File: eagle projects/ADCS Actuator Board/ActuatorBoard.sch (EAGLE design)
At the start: 256 parts, among them J4 OSTVN08A150, J5 OSTVN08A150, J6 OSTVN08A150, U10 TVS991, U11 BD6210F-E2, U12 ADS7841E_2K5, U13 ADS7841E_2K5, U15 TLV9051IDCKR, U16 BD6210F-E2, U17 DRV10970_MOTOR_DRIVERDRV10970, U18 DRV10970_MOTOR_DRIVERDRV10970, U19 TLV9051IDCKR, U20 DRV10970_MOTOR_DRIVERDRV10970, U21 TLV9051IDCKR, U22 BD6210F-E2, U23 TLV9051IDCKR, U24 TLV9051IDCKR, U25 ADS7841E_2K5, U26 TLV9051IDCKR, U27 ADS7841E_2K5, U28 TLV9051IDCKR, U29 TLV9051IDCKR, U30 TLV9051IDCKR, U31 TLV9051IDCKR, U32 TLV9051IDCKR, U4 ADS7841E_2K5, U6 TLV9051IDCKR, U7 TVS991, U8 TVS991, U9 ADS7841E_2K5

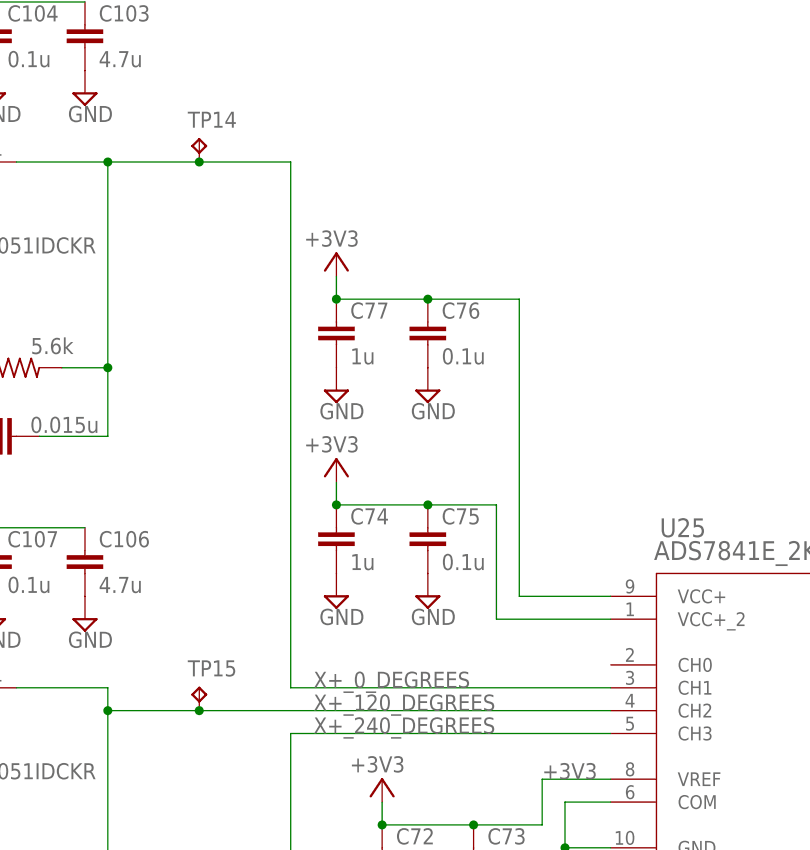
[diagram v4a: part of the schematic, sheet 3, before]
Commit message: finished rearranging analog side for minimal a/d ground bridge spacing
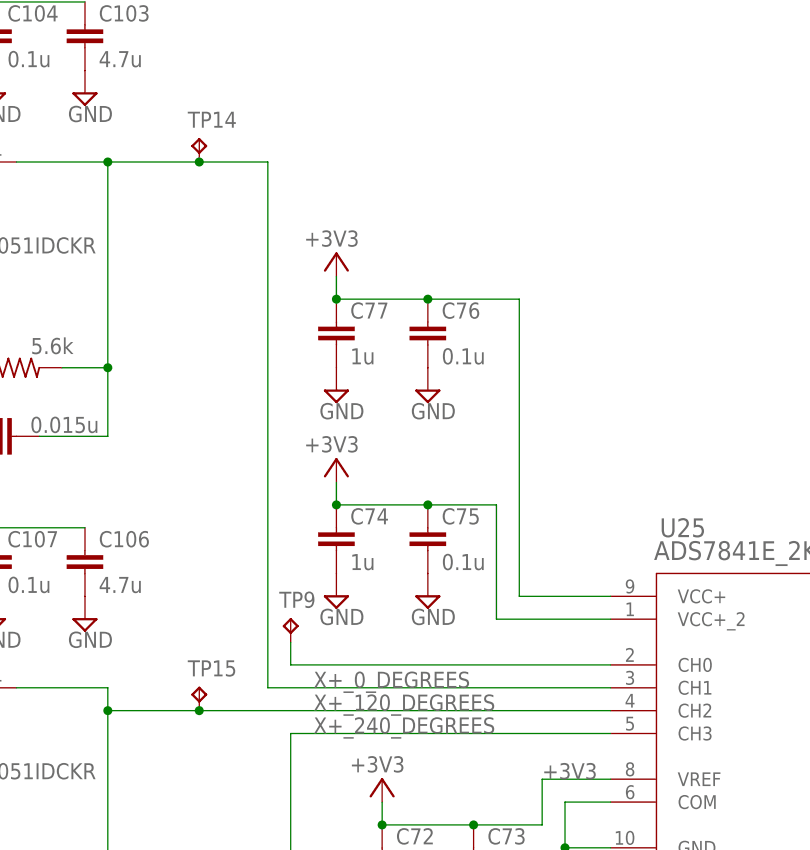
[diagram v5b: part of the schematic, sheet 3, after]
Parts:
- added TP1, TP13, TP17, TP9: TESTPOINT, my_library:TESTPOINT
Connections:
- new net N$1: TP1.TP, U13.CH0
- new net N$2: TP9.TP, U25.CH0
- new net N$3: TP13.TP, U27.CH0
- new net N$9: TP17.TP, U4.CH0
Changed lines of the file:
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@@
 <part name="R5" library="rcl" library_urn="urn:adsk.eagle:library:334" deviceset="R-US_" device="R0402" package3d_urn="urn:adsk.eagle:package:23547/3" value="10k"/>
 <part name="R6" library="rcl" library_urn="urn:adsk.eagle:library:334" deviceset="R-US_" device="R0402" package3d_urn="urn:adsk.eagle:package:23547/3" value="10k"/>
-<part name="JX" library="my_library" library_urn="urn:adsk.eagle:library:22876504" deviceset="TRM_BLK_1X2" device="" package3d_urn="urn:adsk.eagle:package:9320/1"/>
-<part name="JY" library="my_library" library_urn="urn:adsk.eagle:library:22876504" deviceset="TRM_BLK_1X2" device="" package3d_urn="urn:adsk.eagle:package:9320/1"/>
-<part name="JZ" library="my_library" library_urn="urn:adsk.eagle:library:22876504" deviceset="TRM_BLK_1X2" device="" package3d_urn="urn:adsk.eagle:package:9320/1"/>
+<part name="JX" library="my_library" library_urn="urn:adsk.eagle:library:22876504" deviceset="TRM_BLK_1X2" device="" package3d_urn="urn:adsk.eagle:package:26488321/2"/>
+<part name="JY" library="my_library" library_urn="urn:adsk.eagle:library:22876504" deviceset="TRM_BLK_1X2" device="" package3d_urn="urn:adsk.eagle:package:26488321/2"/>
+<part name="JZ" library="my_library" library_urn="urn:adsk.eagle:library:22876504" deviceset="TRM_BLK_1X2" device="" package3d_urn="urn:adsk.eagle:package:26488321/2"/>
 <part name="+3V4" library="supply1" library_urn="urn:adsk.eagle:library:371" deviceset="+3V3" device=""/>
 <part name="+3V6" library="supply1" library_urn="urn:adsk.eagle:library:371" deviceset="+3V3" device=""/>
@@
 <part name="C6" library="resistor" library_urn="urn:adsk.eagle:library:348" deviceset="C-EU" device="C0402" package3d_urn="urn:adsk.eagle:package:23626/2" value="4.7u"/>
 <part name="C7" library="resistor" library_urn="urn:adsk.eagle:library:348" deviceset="C-EU" device="C0402" package3d_urn="urn:adsk.eagle:package:23626/2" value="4.7u"/>
-<part name="J7" library="my_library" library_urn="urn:adsk.eagle:library:22876504" deviceset="TRM_BLK_1X2" device="" package3d_urn="urn:adsk.eagle:package:9320/1"/>
+<part name="J7" library="my_library" library_urn="urn:adsk.eagle:library:22876504" deviceset="TRM_BLK_1X2" device="" package3d_urn="urn:adsk.eagle:package:26488321/2"/>
+<part name="TP1" library="my_library" library_urn="urn:adsk.eagle:library:22876504" deviceset="TESTPOINT" device="" package3d_urn="urn:adsk.eagle:package:24605432/2"/>
+<part name="TP9" library="my_library" library_urn="urn:adsk.eagle:library:22876504" deviceset="TESTPOINT" device="" package3d_urn="urn:adsk.eagle:package:24605432/2"/>
+<part name="TP13" library="my_library" library_urn="urn:adsk.eagle:library:22876504" deviceset="TESTPOINT" device="" package3d_urn="urn:adsk.eagle:package:24605432/2"/>
+<part name="TP17" library="my_library" library_urn="urn:adsk.eagle:library:22876504" deviceset="TESTPOINT" device="" package3d_urn="urn:adsk.eagle:package:24605432/2"/>
 </parts>
 <sheets>
@@
 <attribute name="VALUE" x="240.03" y="98.298" size="1.778" layer="96"/>
 </instance>
+<instance part="TP9" gate="G$1" x="129.54" y="121.92" smashed="yes">
+<attribute name="NAME" x="128.27" y="123.19" size="1.778" layer="95"/>
+</instance>
 </instances>
 <busses>
@@
 <segment>
 <label x="132.08" y="114.3" size="1.778" layer="95"/>
-<wire x1="129.54" y1="172.72" x2="129.54" y2="114.3" width="0.1524" layer="91"/>
 <pinref part="U26" gate="G$1" pin="OUT"/>
 <wire x1="99.06" y1="172.72" x2="109.22" y2="172.72" width="0.1524" layer="91"/>
 <pinref part="R55" gate="G$1" pin="2"/>
 <wire x1="109.22" y1="172.72" x2="119.38" y2="172.72" width="0.1524" layer="91"/>
-<wire x1="119.38" y1="172.72" x2="129.54" y2="172.72" width="0.1524" layer="91"/>
+<wire x1="119.38" y1="172.72" x2="127" y2="172.72" width="0.1524" layer="91"/>
 <wire x1="104.14" y1="149.86" x2="109.22" y2="149.86" width="0.1524" layer="91"/>
 <wire x1="109.22" y1="149.86" x2="109.22" y2="172.72" width="0.1524" layer="91"/>
@@
 <wire x1="109.22" y1="142.24" x2="101.6" y2="142.24" width="0.1524" layer="91"/>
 <pinref part="U25" gate="A" pin="CH1"/>
-<wire x1="165.1" y1="114.3" x2="129.54" y2="114.3" width="0.1524" layer="91"/>
+<wire x1="165.1" y1="114.3" x2="127" y2="114.3" width="0.1524" layer="91"/>
+<wire x1="127" y1="114.3" x2="127" y2="172.72" width="0.1524" layer="91"/>
 </segment>
 </net>
@@
 </segment>
 </net>
+<net name="N$2" class="0">
+<segment>
+<pinref part="TP9" gate="G$1" pin="TP"/>
+<wire x1="129.54" y1="119.38" x2="129.54" y2="116.84" width="0.1524" layer="91"/>
+<pinref part="U25" gate="A" pin="CH0"/>
+<wire x1="129.54" y1="116.84" x2="165.1" y2="116.84" width="0.1524" layer="91"/>
+</segment>
+</net>
 </nets>
 </sheet>
@@
 <attribute name="VALUE" x="248.92" y="111.76" size="1.778" layer="96" rot="R180"/>
 </instance>
+<instance part="TP1" gate="G$1" x="121.92" y="124.46" smashed="yes">
+<attribute name="NAME" x="120.65" y="125.73" size="1.778" layer="95"/>
+</instance>
 </instances>
 <busses>
@@
 <segment>
 <label x="127" y="114.3" size="1.778" layer="95"/>
-<wire x1="124.46" y1="172.72" x2="124.46" y2="114.3" width="0.1524" layer="91"/>
+<wire x1="119.38" y1="172.72" x2="119.38" y2="114.3" width="0.1524" layer="91"/>
 <pinref part="U15" gate="G$1" pin="OUT"/>
 <wire x1="93.98" y1="172.72" x2="104.14" y2="172.72" width="0.1524" layer="91"/>
 <pinref part="R40" gate="G$1" pin="2"/>
 <wire x1="104.14" y1="172.72" x2="114.3" y2="172.72" width="0.1524" layer="91"/>
-<wire x1="114.3" y1="172.72" x2="124.46" y2="172.72" width="0.1524" layer="91"/>
+<wire x1="114.3" y1="172.72" x2="119.38" y2="172.72" width="0.1524" layer="91"/>
 <wire x1="99.06" y1="149.86" x2="104.14" y2="149.86" width="0.1524" layer="91"/>
 <wire x1="104.14" y1="149.86" x2="104.14" y2="172.72" width="0.1524" layer="91"/>
@@
 <wire x1="104.14" y1="142.24" x2="96.52" y2="142.24" width="0.1524" layer="91"/>
 <pinref part="U13" gate="A" pin="CH1"/>
-<wire x1="160.02" y1="114.3" x2="124.46" y2="114.3" width="0.1524" layer="91"/>
+<wire x1="160.02" y1="114.3" x2="119.38" y2="114.3" width="0.1524" layer="91"/>
 </segment>
 </net>
@@
 </segment>
 </net>
+<net name="N$1" class="0">
+<segment>
+<pinref part="U13" gate="A" pin="CH0"/>
+<wire x1="160.02" y1="116.84" x2="121.92" y2="116.84" width="0.1524" layer="91"/>
+<wire x1="121.92" y1="116.84" x2="121.92" y2="121.92" width="0.1524" layer="91"/>
+<pinref part="TP1" gate="G$1" pin="TP"/>
+</segment>
+</net>
 </nets>
 </sheet>
@@
 <attribute name="VALUE" x="121.92" y="165.1" size="1.778" layer="96" rot="R180"/>
 </instance>
+<instance part="TP13" gate="G$1" x="111.76" y="121.92" smashed="yes">
+<attribute name="NAME" x="110.49" y="123.19" size="1.778" layer="95"/>
+</instance>
 </instances>
 <busses>
@@
 <segment>
 <label x="116.84" y="114.3" size="1.778" layer="95"/>
-<wire x1="114.3" y1="172.72" x2="114.3" y2="114.3" width="0.1524" layer="91"/>
+<wire x1="109.22" y1="172.72" x2="109.22" y2="114.3" width="0.1524" layer="91"/>
 <pinref part="U30" gate="G$1" pin="OUT"/>
 <wire x1="83.82" y1="172.72" x2="93.98" y2="172.72" width="0.1524" layer="91"/>
 <pinref part="R64" gate="G$1" pin="2"/>
 <wire x1="93.98" y1="172.72" x2="104.14" y2="172.72" width="0.1524" layer="91"/>
-<wire x1="104.14" y1="172.72" x2="114.3" y2="172.72" width="0.1524" layer="91"/>
+<wire x1="104.14" y1="172.72" x2="109.22" y2="172.72" width="0.1524" layer="91"/>
 <wire x1="88.9" y1="149.86" x2="93.98" y2="149.86" width="0.1524" layer="91"/>
 <wire x1="93.98" y1="149.86" x2="93.98" y2="172.72" width="0.1524" layer="91"/>
@@
 <wire x1="93.98" y1="142.24" x2="86.36" y2="142.24" width="0.1524" layer="91"/>
 <pinref part="U27" gate="A" pin="CH1"/>
-<wire x1="149.86" y1="114.3" x2="114.3" y2="114.3" width="0.1524" layer="91"/>
+<wire x1="149.86" y1="114.3" x2="109.22" y2="114.3" width="0.1524" layer="91"/>
 </segment>
 </net>
@@
 </segment>
 </net>
+<net name="N$3" class="0">
+<segment>
+<pinref part="U27" gate="A" pin="CH0"/>
+<wire x1="149.86" y1="116.84" x2="111.76" y2="116.84" width="0.1524" layer="91"/>
+<pinref part="TP13" gate="G$1" pin="TP"/>
+<wire x1="111.76" y1="116.84" x2="111.76" y2="119.38" width="0.1524" layer="91"/>
+</segment>
+</net>
 </nets>
 </sheet>
@@
 <attribute name="VALUE" x="42.164" y="86.995" size="1.778" layer="96" rot="R180"/>
 </instance>
+<instance part="TP17" gate="G$1" x="116.84" y="124.46" smashed="yes">
+<attribute name="NAME" x="115.57" y="125.73" size="1.778" layer="95"/>
+</instance>
 </instances>
 <busses>
@@
 <segment>
 <label x="121.92" y="116.84" size="1.778" layer="95"/>
-<wire x1="119.38" y1="175.26" x2="119.38" y2="116.84" width="0.1524" layer="91"/>
+<wire x1="114.3" y1="175.26" x2="114.3" y2="116.84" width="0.1524" layer="91"/>
 <pinref part="U6" gate="G$1" pin="OUT"/>
 <wire x1="88.9" y1="175.26" x2="99.06" y2="175.26" width="0.1524" layer="91"/>
 <pinref part="R24" gate="G$1" pin="2"/>
 <wire x1="99.06" y1="175.26" x2="109.22" y2="175.26" width="0.1524" layer="91"/>
-<wire x1="109.22" y1="175.26" x2="119.38" y2="175.26" width="0.1524" layer="91"/>
+<wire x1="109.22" y1="175.26" x2="114.3" y2="175.26" width="0.1524" layer="91"/>
 <wire x1="93.98" y1="152.4" x2="99.06" y2="152.4" width="0.1524" layer="91"/>
 <wire x1="99.06" y1="152.4" x2="99.06" y2="175.26" width="0.1524" layer="91"/>
@@
 <wire x1="99.06" y1="144.78" x2="91.44" y2="144.78" width="0.1524" layer="91"/>
 <pinref part="U4" gate="A" pin="CH1"/>
-<wire x1="154.94" y1="116.84" x2="119.38" y2="116.84" width="0.1524" layer="91"/>
+<wire x1="154.94" y1="116.84" x2="114.3" y2="116.84" width="0.1524" layer="91"/>
 </segment>
 </net>
@@
 </segment>
 </net>
+<net name="N$9" class="0">
+<segment>
+<pinref part="TP17" gate="G$1" pin="TP"/>
+<wire x1="116.84" y1="121.92" x2="116.84" y2="119.38" width="0.1524" layer="91"/>
+<pinref part="U4" gate="A" pin="CH0"/>
+<wire x1="116.84" y1="119.38" x2="154.94" y2="119.38" width="0.1524" layer="91"/>
+</segment>
+</net>

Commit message: fixed silkscreen fiasco
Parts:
- removed D1, D10, D11, D12, D13, D14, D15, D3, D5, D7, D8, D9: SFH2430, my_library:SFH2430
- added J10, J11, J12, J13, J14, J15, J16, J17, J18, J8, J9: (no value), my_library:TRM_BLK_1X2
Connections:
- removed net N$33: C100.1, D3.C, R31.1, U23.-
- removed net N$60: C98.1, D13.C, R64.1, U30.-
- new net N$23: C100.1, J7.2, R31.1, U23.-
- new net N$37: C98.1, J12.2, R64.1, U30.-
- net GND: now also J10.1, J11.1, J12.1, J13.1, J14.1, J15.1, J16.1, J17.1, J18.1, J7.1, J8.1, J9.1; no longer D1.A, D10.A, D11.A, D12.A, D13.A, D14.A, D15.A, D3.A, D5.A, D7.A, D8.A, D9.A
- net N$29: now also J8.2; no longer D1.C
- net N$35: now also J9.2; no longer D5.C
- net N$38: now also J15.2; no longer D7.C
- net N$44: now also J14.2; no longer D8.C
- net N$46: now also J13.2; no longer D9.C
- net N$49: now also J18.2; no longer D10.C
- net N$55: now also J17.2; no longer D11.C
- net N$57: now also J16.2; no longer D12.C
- net N$63: now also J11.2; no longer D14.C
- net N$65: now also J10.2; no longer D15.C
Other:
- moved on the sheet: J7

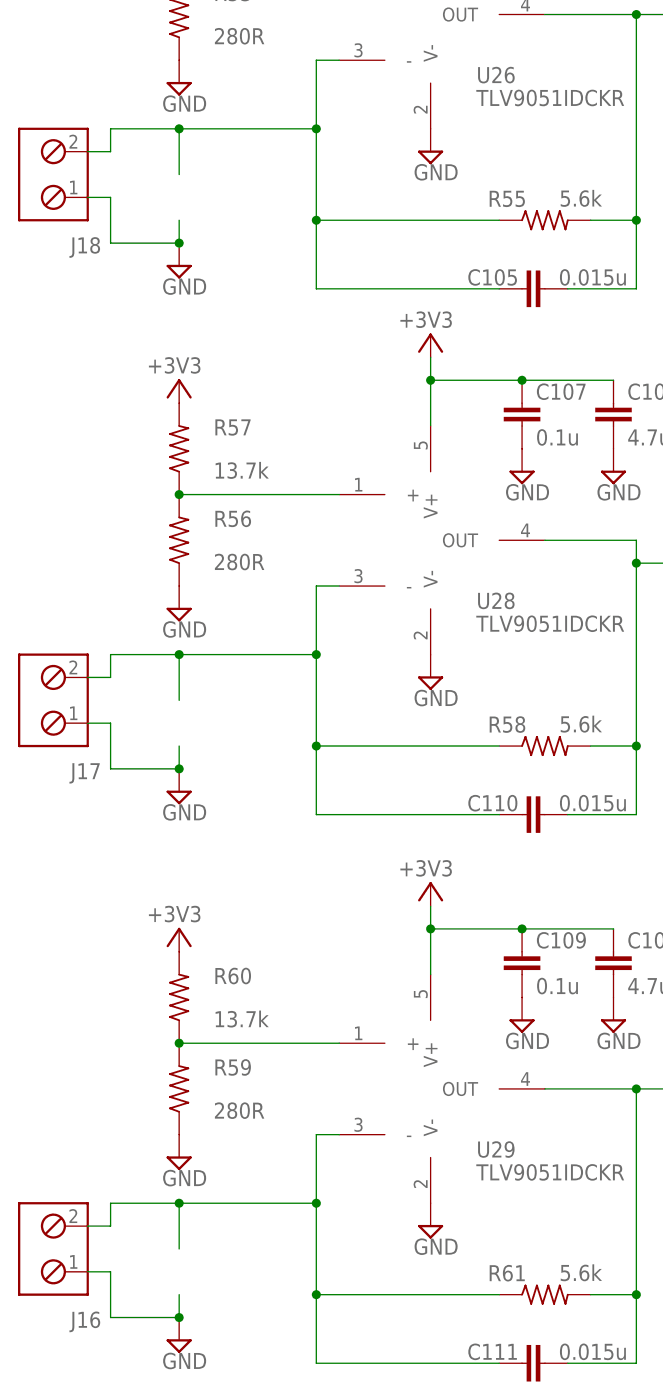
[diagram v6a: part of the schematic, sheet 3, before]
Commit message: Added photodiode symbols without footprint and replaced title blocks
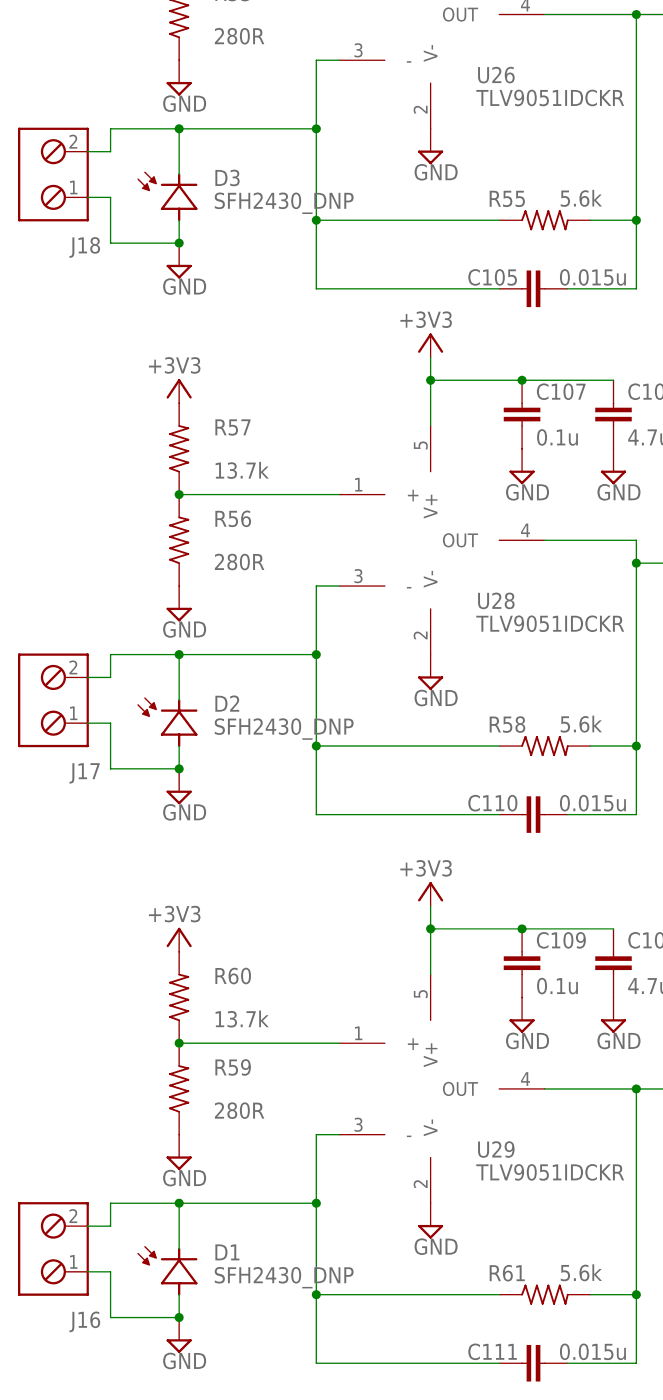
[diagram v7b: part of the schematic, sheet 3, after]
